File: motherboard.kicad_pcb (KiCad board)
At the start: 2 copper layers, 90.2 x 95.9 mm, 107 parts, among them P1 CONN_02X08, U1 STM32F411-LQFP64, U10 74LS125, U11 74LS125, U12 74LS125, U13 74LS125, U14 PCA9517A, U15 PCA9517A, U16 74LS125, U17 74LS125, U2 STM32F411-LQFP64, U3 AP7313, U4 74LS00, U5 74LS125, U6 FM25V20A-G, U7 FM25V20A-G, U8 FM25V20A-G, U9 FM25V20A-G, Y1 32k, Y2 8M(16pF), Y3 32k, Y4 8M(16pF)

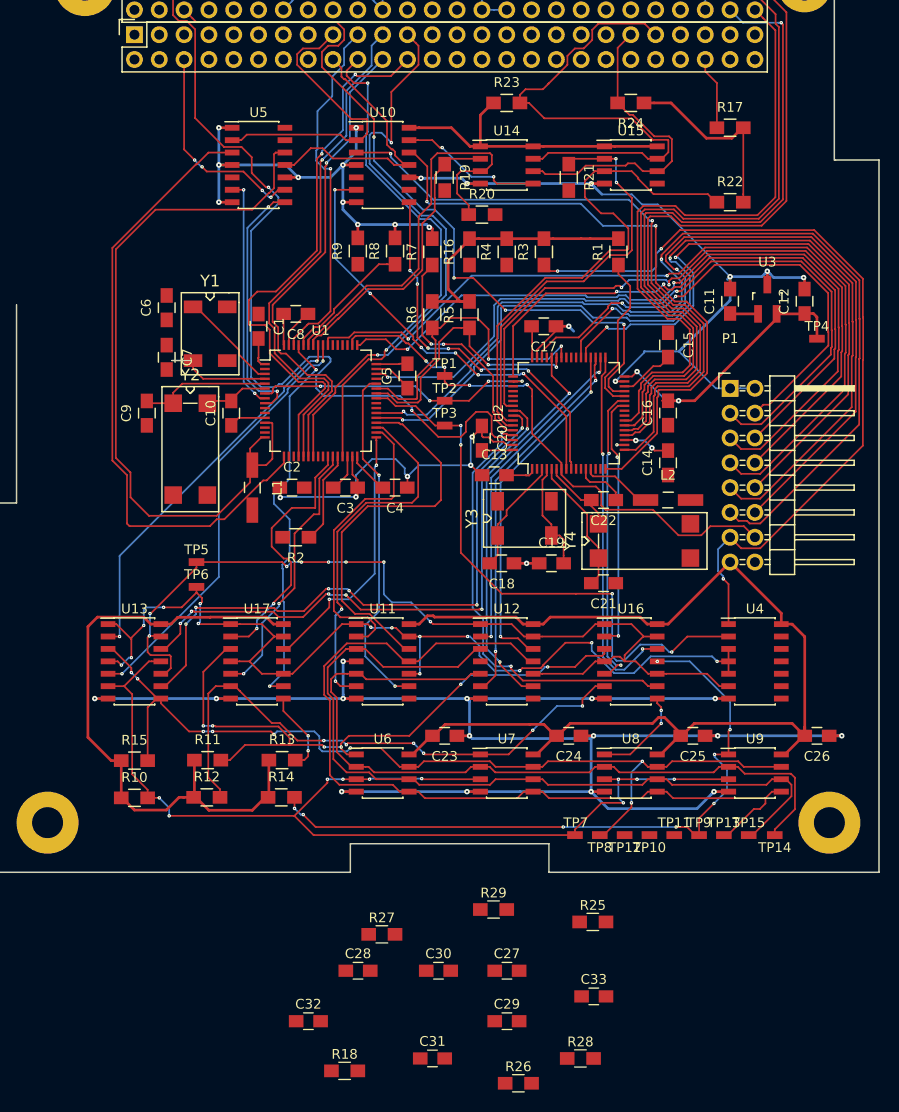
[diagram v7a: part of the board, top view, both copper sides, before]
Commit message: All components placed
Most signals routed
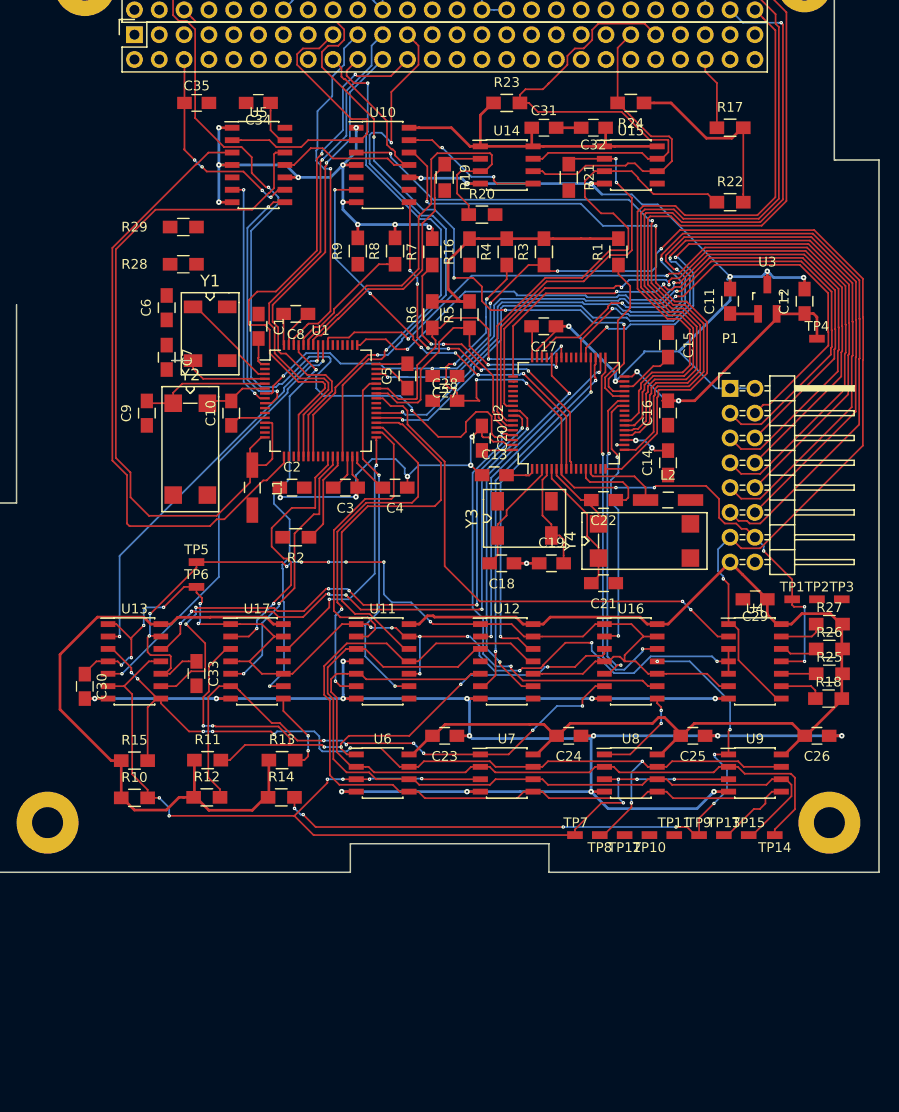
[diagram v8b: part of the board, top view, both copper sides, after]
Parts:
- added C34: 0.1uF, Capacitors_SMD:C_0805_HandSoldering, F.Cu at (139.7, 63.5)
- added C35: 0.1uF, Capacitors_SMD:C_0805_HandSoldering, F.Cu at (133.4, 63.5)
- moved C32 96.0 mm to (174.0, 66.0), turned to 180 degrees
- moved C31 95.9 mm to (168.9, 66.0)
- moved R28 90.9 mm to (132.0, 80.0)
- moved R29 76.7 mm to (132.0, 76.2)
- moved R18 62.5 mm to (198.0, 124.5)
- moved C27 61.2 mm to (158.8, 91.4), turned to 180 degrees
- moved C28 59.0 mm to (158.8, 94.0)
- moved R27 55.7 mm to (198.1, 116.8)
- moved R26 54.7 mm to (198.1, 119.4)
- moved C33 52.4 mm to (133.3, 121.9), turned to 270 degrees
- moved C29 50.1 mm to (190.5, 114.3), turned to 180 degrees
- moved C30 46.4 mm to (121.9, 123.2), turned to 270 degrees
- moved TP3 44.4 mm to (199.4, 114.3)
- moved TP2 43.2 mm to (196.8, 114.3)
- moved TP1 42.3 mm to (194.3, 114.3)
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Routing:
- net /NRST_S: track 46.1 -> 79.7 mm, vias 3 -> 9
- net /NRST_P: track 107.7 -> 131.5 mm, vias 5 -> 6
- net /SGPIO8: track 38.3 -> 20.9 mm, vias 2 -> 1
- net /I2C2_SCL: track 13.3 -> 30.8 mm, vias 0 -> 1
- net GND: track 451.1 -> 464.2 mm
- net +3V3: track 273.3 -> 286.2 mm
- net Net-(H1-Pad24): track 25.8 -> 15.9 mm
- net /SYS_SPI_NSS: track 31.8 -> 41.7 mm
- net /NBUFEN_PRI: track 101.9 -> 109.8 mm
- net /NYIELD_P: track 60.2 -> 53.2 mm, vias 4 -> 2
- net /SGPIO7: track 16.5 -> 9.53 mm
- net /I2C2_SDA: track 20.2 -> 27.1 mm
- net /NRST1_S: track 10.3 -> 4.33 mm, vias 1 -> 0
- net /NRST2_S: track 0.00 -> 4.58 mm
- net /NBUFEN_SEC: track 138.0 -> 142.2 mm
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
